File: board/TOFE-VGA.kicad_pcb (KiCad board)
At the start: 4 copper layers, 46 x 3 mm, 114 parts, among them P1 CONN_02X06, P301 TOFE I2C, P302 TOFE-8X, P303 DEBUG, P401 AD9984 I2C, P501 VGA RX I2C 3v, P502 VGA TX I2C 3v, P503 VGA RX I2C 5v, P504 VGA TX I2C 5v, P505 DE-15, P506 DE-15, P601 3-RCA, U201 ADP3334, U202 ADP3334, U203 LP2985, U301 24AA01/24LC01B, U401 AD9984, U501 TCA9617A, U502 TCA9617A

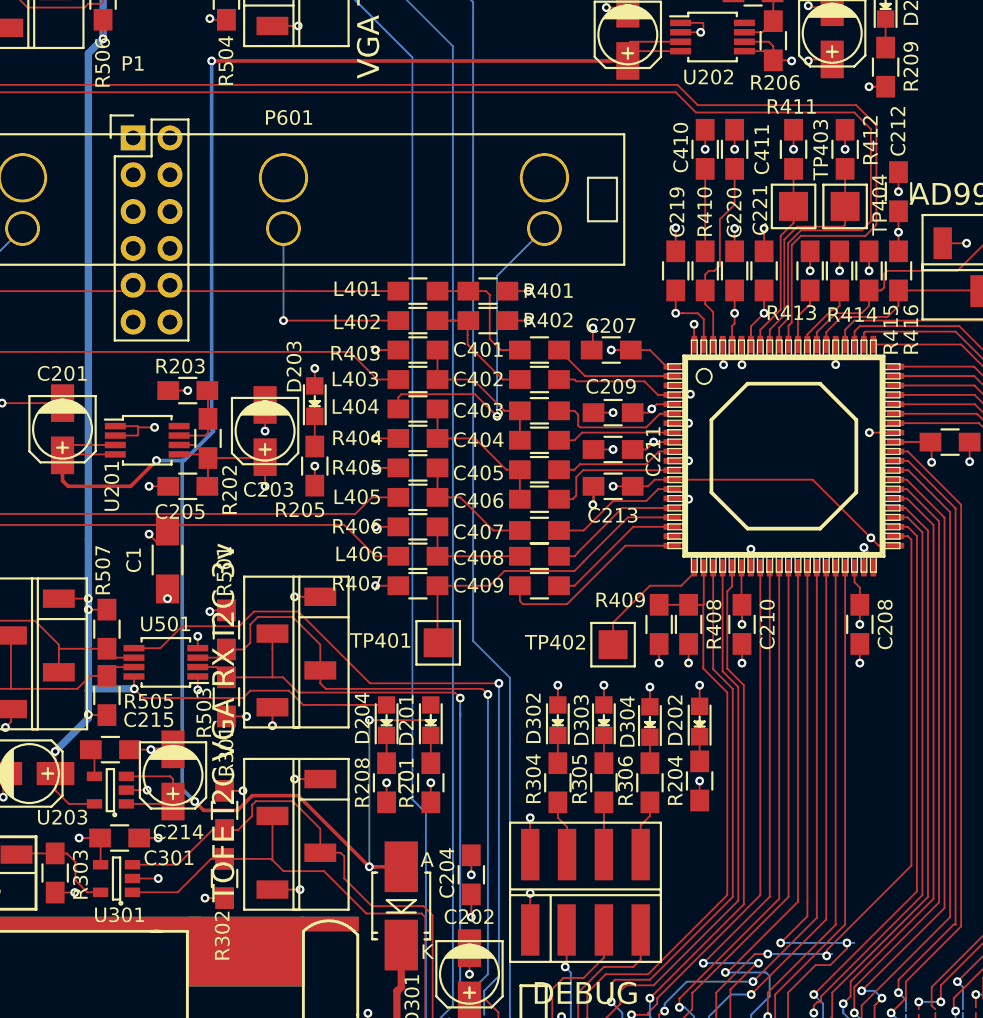
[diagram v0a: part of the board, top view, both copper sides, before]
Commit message: Lots of small tweaks.
 * Giving things better reference names.
 * Giving a bunch of nets names.
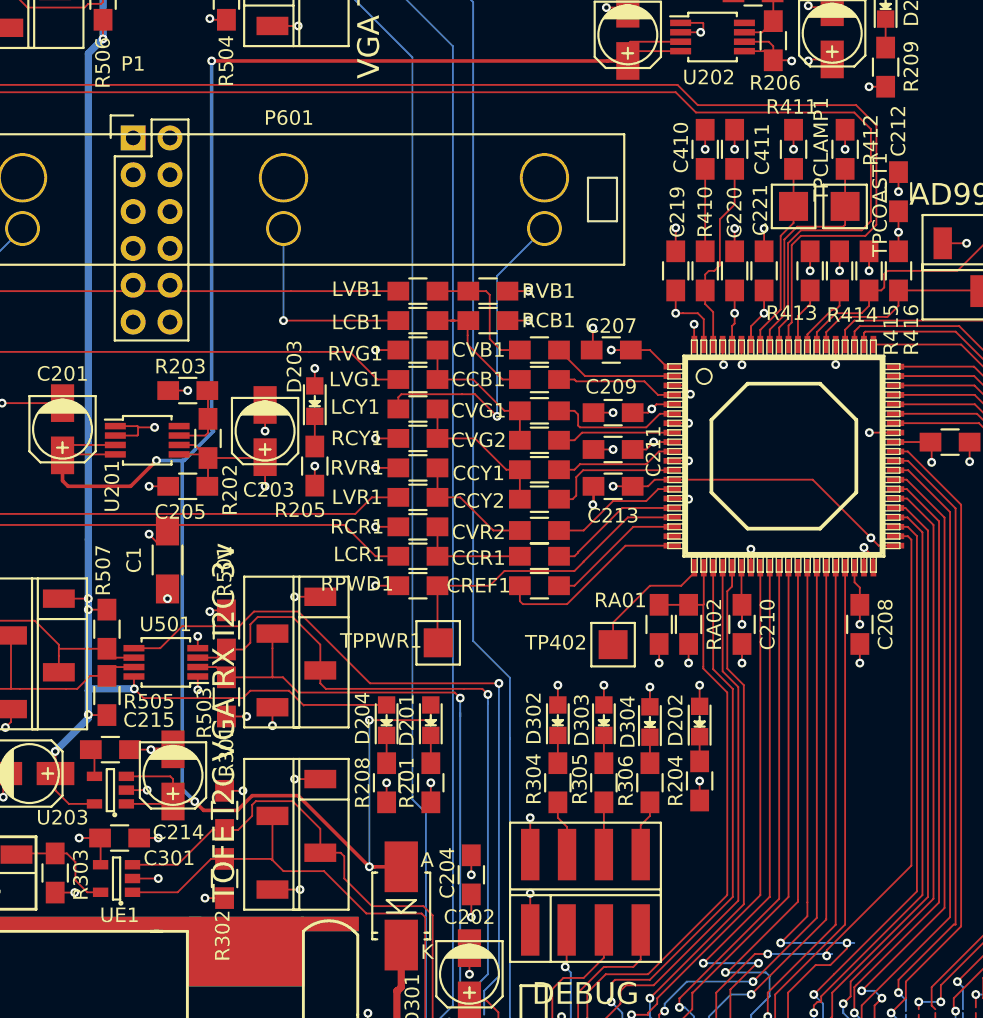
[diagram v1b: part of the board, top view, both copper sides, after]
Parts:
- C410: value 82n -> 80n
- C411: value 8.2n -> 8.0n
- CCY2: renamed from C406; value 47n -> 1n
- CREF1: renamed from C409; value 10n -> 10u
- CVG2: renamed from C404; value 47n -> 1n
- renumbered C402 to CCB1, C408 to CCR1, C405 to CCY1, C401 to CVB1, C403 to CVG1, C407 to CVR2, L402 to LCB1, L406 to LCR1, L404 to LCY1, L401 to LVB1, L403 to LVG1, L405 to LVR1, P301 to PTI2C1, R409 to RA01, R408 to RA02, R402 to RCB1, R406 to RCR1, R404 to RCY1, R407 to RPWD1, R401 to RVB1, R403 to RVG1, R405 to RVR1, TP403 to TPCLAMP1, TP404 to TPCOAST1, TP401 to TPPWR1, U301 to UE1
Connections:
- net Net-(C401-Pad2) renamed /TOFE-VGA/AD9984/VB
- net Net-(C402-Pad2) renamed /TOFE-VGA/AD9984/CB
- net Net-(C403-Pad2) renamed /TOFE-VGA/AD9984/VG
- net Net-(C405-Pad2) renamed /TOFE-VGA/AD9984/CY
- net Net-(C407-Pad2) renamed /TOFE-VGA/AD9984/VR
- net Net-(C408-Pad2) renamed /TOFE-VGA/AD9984/CR
- net Net-(C409-Pad1) renamed /TOFE-VGA/AD9984/REFHI
- net Net-(C409-Pad2) renamed /TOFE-VGA/AD9984/REFLO
- net Net-(R411-Pad1) renamed /TOFE-VGA/AD9984/CLAMP
- net Net-(R412-Pad1) renamed /TOFE-VGA/AD9984/COAST
- C216 pad 2: GND -> GNDA
- C218 pad 2: GND -> GNDA
- C219 pad 2: GND -> GNDA
- C220 pad 2: GND -> GNDA
- C221 pad 2: GND -> GNDA
- P302 pad A11: Net-(P302-PadA11) -> /TOFE-VGA/AD9984/RST
- P302 pad A16: Net-(P302-PadA16) -> /TOFE-VGA/AD9984/FIELD
- P303 pad 1: GND -> Net-(P303-Pad1)
- P303 pad 7: Net-(P302-PadA16) -> Net-(P303-Pad7)
- P303 pad 8: Net-(P303-Pad8) -> GND
- R207 pad 2: GND -> GNDA
- R209 pad 2: GND -> GNDA
- RPWD1 pad 1: Net-(R407-Pad1) -> /TOFE-VGA/AD9984/RST
- TPPWR1 pad 1: Net-(R407-Pad1) -> /TOFE-VGA/AD9984/RST
- U202 pad 1: GND -> GNDA
- U202 pad 2: GND -> GNDA
- U401 pad 17: Net-(R407-Pad1) -> /TOFE-VGA/AD9984/RST
- U401 pad 21: Net-(TP402-Pad1) -> /TOFE-VGA/AD9984/FIELD
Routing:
- net Net-(R407-Pad1): track 22.5 -> 0.00 mm
- net /TOFE-VGA/AD9984/RST: track 0.00 -> 22.5 mm
- net GNDA: track 83.1 -> 97.1 mm, vias 22 -> 30
- net GND: track 192.7 -> 179.1 mm, vias 66 -> 57
- net Net-(P302-PadA16): track 10.2 -> 0.00 mm
- net Net-(P303-Pad7): track 0.00 -> 10.1 mm
- net /TOFE-VGA/AD9984/FIELD: track 0.00 -> 7.42 mm
- net Net-(TP402-Pad1): track 8.89 -> 1.52 mm
- net Net-(P303-Pad8): track 3.87 -> 0.94 mm
- net Net-(P303-Pad1): track 0.00 -> 2.53 mm, vias 0 -> 1

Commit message: Update to PCB.
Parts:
- C215: value 10n -> C5VI2
- renumbered C214 to C5VI1, C217 to C5VO1, C204 to CIO1, C206 to CIO2, C208 to CIO3, C210 to CIO4, C212 to CIO5, C219 to CPV1, C220 to CPV2, C221 to CPV3, C216 to CPVI1, C218 to CPVO1, C202 to CTIO1, C205 to CVD1, C207 to CVD2, C209 to CVD3, C211 to CVD4, C213 to CVD5, C201 to CVDI1, C203 to CVDO1, D201 to D12V1, D204 to D5V1, D205 to DPV1, D202 to DTIO1, D203 to DVD1, R201 to R12V1, R208 to R5V1, R206 to RPV1, R207 to RPV2, R209 to RPV3, R204 to RTIO1, R202 to RVD1, R203 to RVD2, R205 to RVD3, U203 to U5V1, U202 to UPV1, U201 to UVD1
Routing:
- net Net-(TP402-Pad1): track 1.52 -> 5.12 mm
- net /TOFE-VGA/AD9984/FIELD: track 7.42 -> 3.83 mm

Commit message: Updating net names.
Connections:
- net Net-(C411-Pad2) renamed /TOFE-VGA/AD9984/FILT
- P401 pad 1: Net-(P401-Pad1) -> +3V3
- U401 pad 64: Net-(P401-Pad1) -> +3V3
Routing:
- net Net-(P401-Pad1): track 17.3 -> 0.00 mm
- net +3V3: track 65.2 -> 82.5 mm
- net /TOFE-VGA/AD9984/FIELD: track 3.83 -> 1.67 mm
- net Net-(TP402-Pad1): track 5.12 -> 7.28 mm

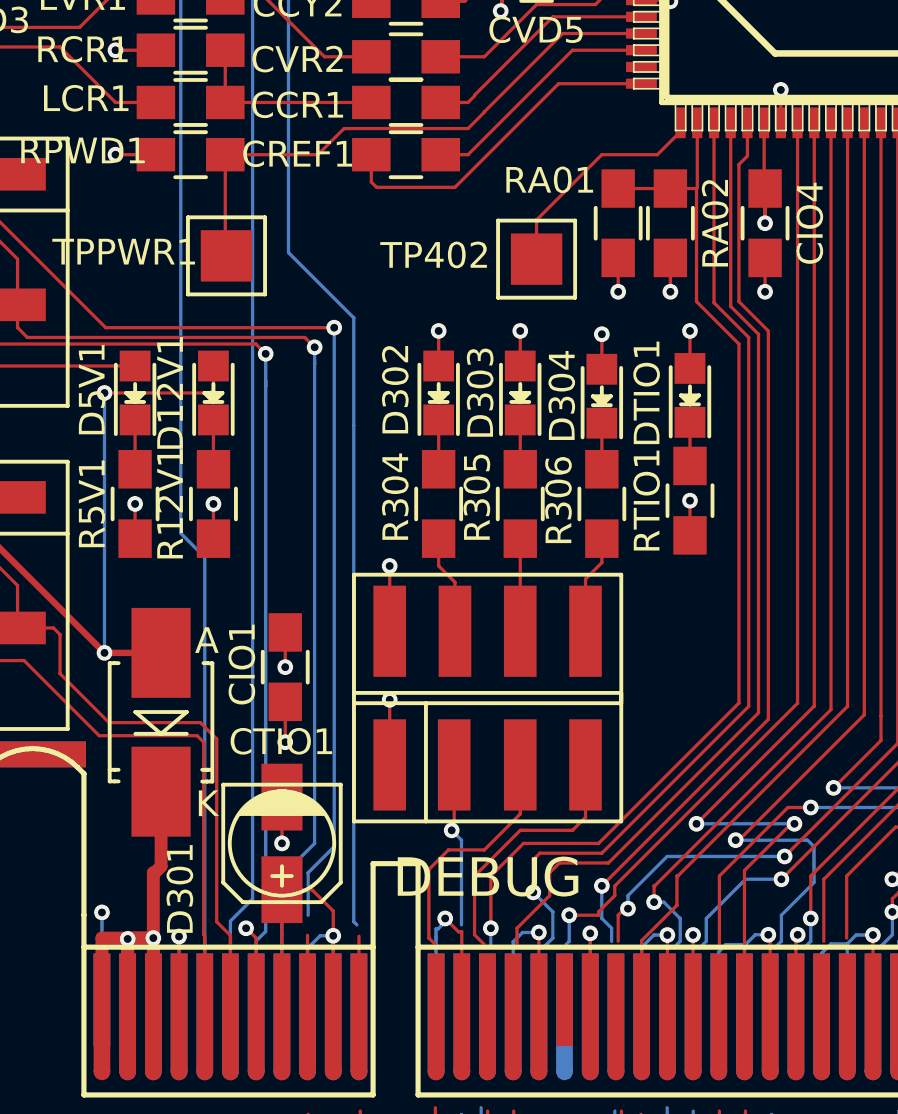
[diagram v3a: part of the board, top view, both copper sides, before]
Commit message: Importing net into PCB.
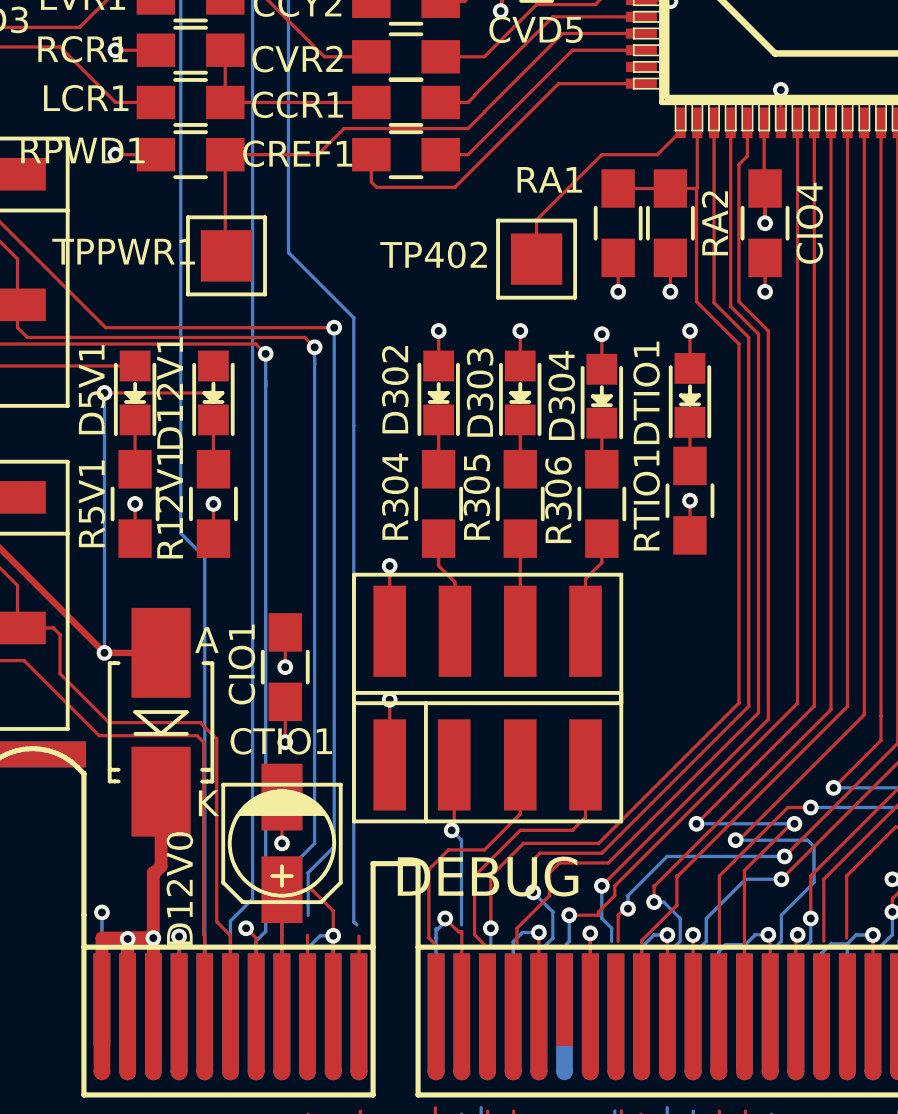
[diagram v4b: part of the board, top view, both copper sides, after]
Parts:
- renumbered D301 to D12V0, RA01 to RA1, RA02 to RA2
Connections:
- net /TOFE-VGA/TOFE/EN_VGA_RX renamed /TOFE-VGA/TOFE/VGAIN_I2C_EN
- net /TOFE-VGA/TOFE/EN_VGA_TX renamed /TOFE-VGA/TOFE/VGAOUT_I2C_EN
- net Net-(D301-Pad1) renamed /TOFE-VGA/TOFE/RAW_VCC12V
- net Net-(P302-PadB5) renamed /TOFE-VGA/TOFE/IDCLK
- net Net-(P302-PadB6) renamed /TOFE-VGA/TOFE/IDDAT
- net Net-(P503-Pad2) renamed /TOFE-VGA/VGA/VGAIN5V_SCL
- net Net-(P503-Pad3) renamed /TOFE-VGA/VGA/VGAIN5V_SDA
- net Net-(P504-Pad2) renamed /TOFE-VGA/VGA/VGAOUT5V_SCL
- net Net-(P504-Pad3) renamed /TOFE-VGA/VGA/VGAOUT5V_SDA
- P302 pad A5: /TOFE-VGA/TOFE/SCL_VGA_TX -> /TOFE-VGA/TOFE/VGAOUT_SCL
- P302 pad A6: /TOFE-VGA/TOFE/SDA_VGA_TX -> /TOFE-VGA/VGA/VGAOUT_SCL
- P302 pad A7: /TOFE-VGA/TOFE/SCL_VGA_RX -> /TOFE-VGA/TOFE/VGAIN_SCL
- P302 pad A8: /TOFE-VGA/TOFE/SDA_VGA_RX -> /TOFE-VGA/TOFE/VGAIN_SDA
- P501 pad 2: /TOFE-VGA/TOFE/SCL_VGA_RX -> /TOFE-VGA/VGA/VGAIN_SCLK
- P501 pad 3: /TOFE-VGA/TOFE/SDA_VGA_RX -> /TOFE-VGA/TOFE/VGAIN_SCL
- P502 pad 2: /TOFE-VGA/TOFE/SCL_VGA_TX -> /TOFE-VGA/VGA/VGAOUT_SCL
- P502 pad 3: /TOFE-VGA/TOFE/SDA_VGA_TX -> /TOFE-VGA/TOFE/VGAOUT_SCL
- R501 pad 2: /TOFE-VGA/TOFE/SDA_VGA_RX -> /TOFE-VGA/TOFE/VGAIN_SCL
- R502 pad 2: /TOFE-VGA/TOFE/SDA_VGA_TX -> /TOFE-VGA/TOFE/VGAOUT_SCL
- R503 pad 2: /TOFE-VGA/TOFE/SCL_VGA_RX -> /TOFE-VGA/VGA/VGAIN_SCLK
- R504 pad 2: /TOFE-VGA/TOFE/SCL_VGA_TX -> /TOFE-VGA/VGA/VGAOUT_SCL
- U501 pad 2: /TOFE-VGA/TOFE/SCL_VGA_RX -> /TOFE-VGA/VGA/VGAIN_SCLK
- U501 pad 3: /TOFE-VGA/TOFE/SDA_VGA_RX -> /TOFE-VGA/TOFE/VGAIN_SCL
- U502 pad 2: /TOFE-VGA/TOFE/SCL_VGA_TX -> /TOFE-VGA/VGA/VGAOUT_SCL
- U502 pad 3: /TOFE-VGA/TOFE/SDA_VGA_TX -> /TOFE-VGA/TOFE/VGAOUT_SCL
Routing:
- net /TOFE-VGA/VGA/VGAOUT_SCL: track 0.00 -> 94.8 mm
- net /TOFE-VGA/TOFE/SDA_VGA_TX: track 91.6 -> 0.00 mm, vias 1 -> 0
- net /TOFE-VGA/TOFE/SCL_VGA_TX: track 87.5 -> 0.00 mm, vias 1 -> 0
- net /TOFE-VGA/TOFE/VGAOUT_SCL: track 0.00 -> 84.3 mm, vias 0 -> 2
- net /TOFE-VGA/TOFE/SDA_VGA_RX: track 52.2 -> 0.00 mm, vias 1 -> 0
- net /TOFE-VGA/TOFE/VGAIN_SCL: track 0.00 -> 51.7 mm, vias 0 -> 1
- net /TOFE-VGA/TOFE/SCL_VGA_RX: track 48.1 -> 0.00 mm, vias 1 -> 0
- net /TOFE-VGA/TOFE/VGAIN_SDA: track 0.00 -> 26.5 mm, vias 0 -> 1
- net /TOFE-VGA/VGA/VGAIN_SCLK: track 0.00 -> 22.0 mm

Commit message: Updating the PCB.
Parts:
- renumbered P302 to TOFE0
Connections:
- net /TOFE-VGA/AD9984/HSYNC0 renamed /TOFE-VGA/VGA/VGAIN_HSYNC
- net /TOFE-VGA/VGA/VGAIN_VSYNC0 renamed /TOFE-VGA/VGA/VGAIN_VSYNC
- net /TOFE-VGA/VGA/VGAOUT_HSYNC0 renamed /TOFE-VGA/VGA/VGAOUT_HSYNC
- net /TOFE-VGA/VGA/VGAOUT_VSYNC0 renamed /TOFE-VGA/VGA/VGAOUT_VSYNC
- P501 pad 2: /TOFE-VGA/VGA/VGAIN_SCLK -> /TOFE-VGA/VGA/VGAIN_SCL
- R503 pad 2: /TOFE-VGA/VGA/VGAIN_SCLK -> /TOFE-VGA/VGA/VGAIN_SCL
- TOFE0 pad A8: /TOFE-VGA/TOFE/VGAIN_SDA -> /TOFE-VGA/VGA/VGAIN_SCL
- U501 pad 2: /TOFE-VGA/VGA/VGAIN_SCLK -> /TOFE-VGA/VGA/VGAIN_SCL
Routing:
- net /TOFE-VGA/VGA/VGAIN_SCL: track 0.00 -> 27.3 mm
- net /TOFE-VGA/TOFE/VGAIN_SDA: track 26.5 -> 0.00 mm, vias 1 -> 0
- net /TOFE-VGA/VGA/VGAIN_SCLK: track 22.0 -> 0.00 mm
- net /TOFE-VGA/TOFE/VGAIN_SCL: track 51.7 -> 73.0 mm, vias 1 -> 2
- net /TOFE-VGA/VGA/VGAOUT_SCL: track 94.8 -> 81.6 mm
- net /TOFE-VGA/TOFE/VGAOUT_SCL: track 84.3 -> 97.6 mm

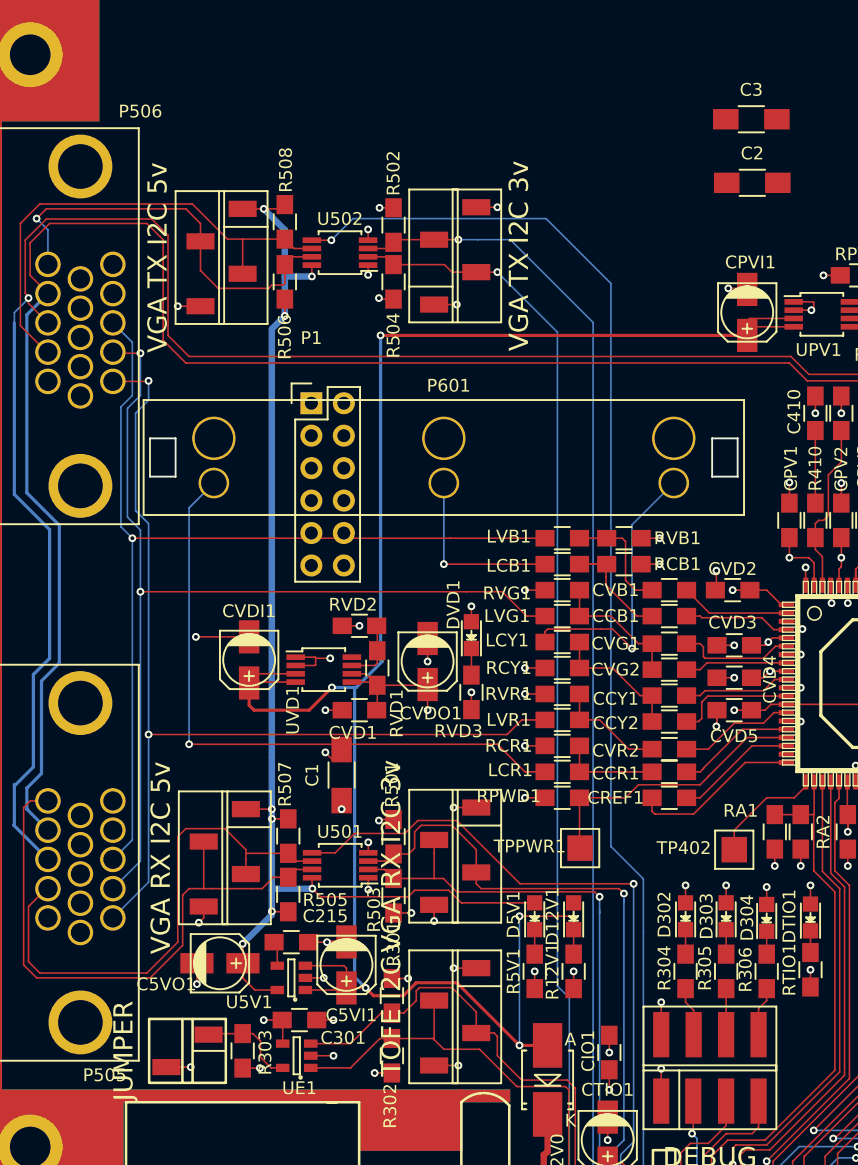
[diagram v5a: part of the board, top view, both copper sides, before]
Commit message: Updating PCB.
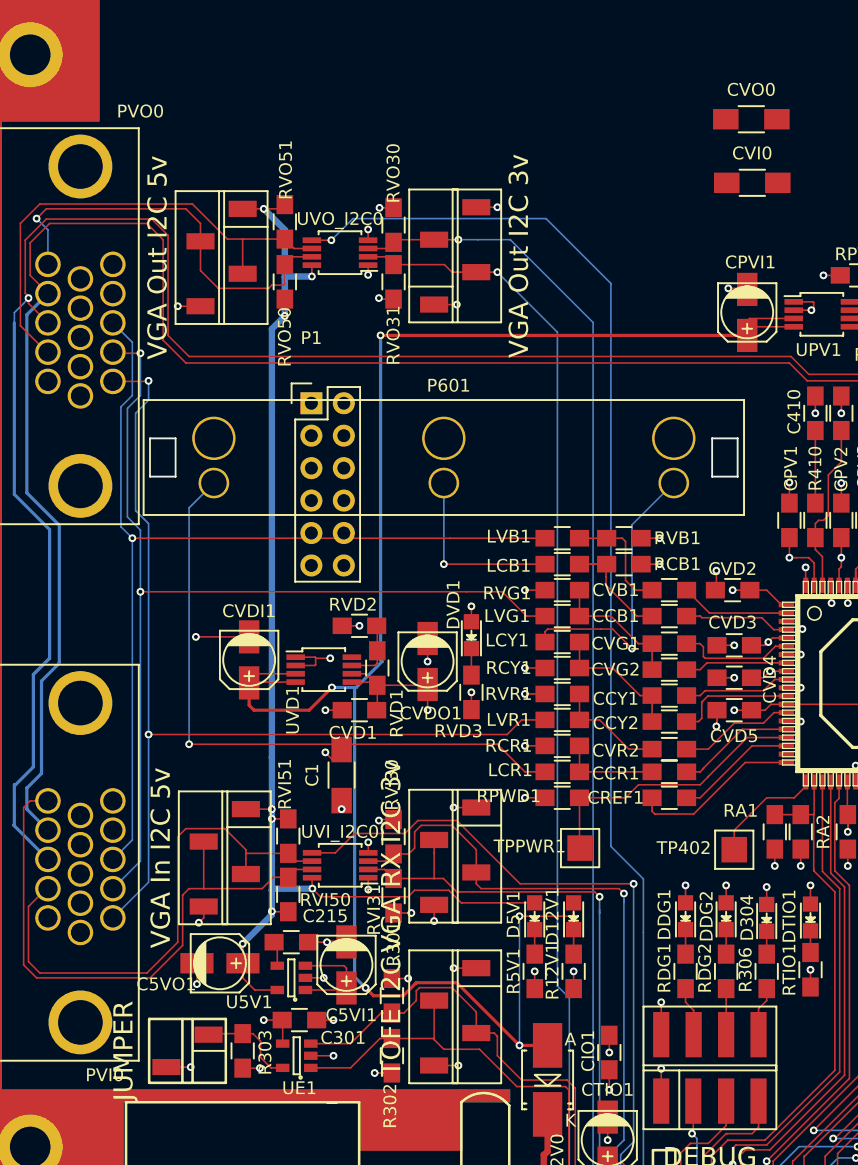
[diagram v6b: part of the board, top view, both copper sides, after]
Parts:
- PVI_I2C5: renamed from P503; value VGA RX I2C 5v -> VGA In I2C 5v
- PVO_I2C3: renamed from P502; value VGA TX I2C 3v -> VGA Out I2C 3v
- PVO_I2C5: renamed from P504; value VGA TX I2C 5v -> VGA Out I2C 5v
- renumbered C2 to CVI0, C3 to CVO0, D302 to DDG1, D303 to DDG2, P401 to PAD_I2C0, P303 to PDG0, P505 to PVI0, P501 to PVI_I2C3, P506 to PVO0, R304 to RDG1, R305 to RDG2, R501 to RVI30, R503 to RVI31, R505 to RVI50, R507 to RVI51, R502 to RVO30, R504 to RVO31, R506 to RVO50, R508 to RVO51, U401 to UAD9984, U501 to UVI_I2C0, U502 to UVO_I2C0
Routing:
- net /TOFE-VGA/TOFE/VGAOUT_SCL: track 97.6 -> 164.9 mm
- net /TOFE-VGA/VGA/VGAOUT_SCL: track 81.6 -> 14.2 mm
